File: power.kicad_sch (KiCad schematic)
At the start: 39 parts

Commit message: Annotate schematic
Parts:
- gave numbers to parts that had none: 39
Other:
- moved on the sheet: TP203

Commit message: Clean up BOM
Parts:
- removed C205, C206, C207, C208: 1mF, symbol Device:C
- added C205, C206, C207, C208: 1mF, symbol Device:C_Polarized
- C201: value 100u -> 100uF
- C202: value 470u -> 470uF
- C203, C209, C215, C216, C217, C219: value 100n -> 100nF
- C204, C213: value 1u -> 1uF
- C210: value 1000u -> 1mF
- C211: value 330u -> 330uF
- C212: value 1.5n -> 1nF
- C214: value 10n -> 10nF
- C220: value 4.7u -> 4.7uF
- L201: value 68uH -> 47uH
- renumbered TP202 to TP201, TP201 to TP202
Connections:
- net +12V: now also C209.1, C210.1, C212.2, L201.2, R202.2, TP204.1; no longer F201.1
- net +BATT: now also F201.1, C205.1, C206.1, C207.1, C208.1; no longer C201.1, C203.1, TP202.1, U201.1 (VIN)
- net GND: now also C205.2, C206.2, C207.2, C208.2
- new net: C201.1, C203.1, F201.2, TP202.1, U201.1 (VIN)
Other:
- moved on the sheet: F201, TP202

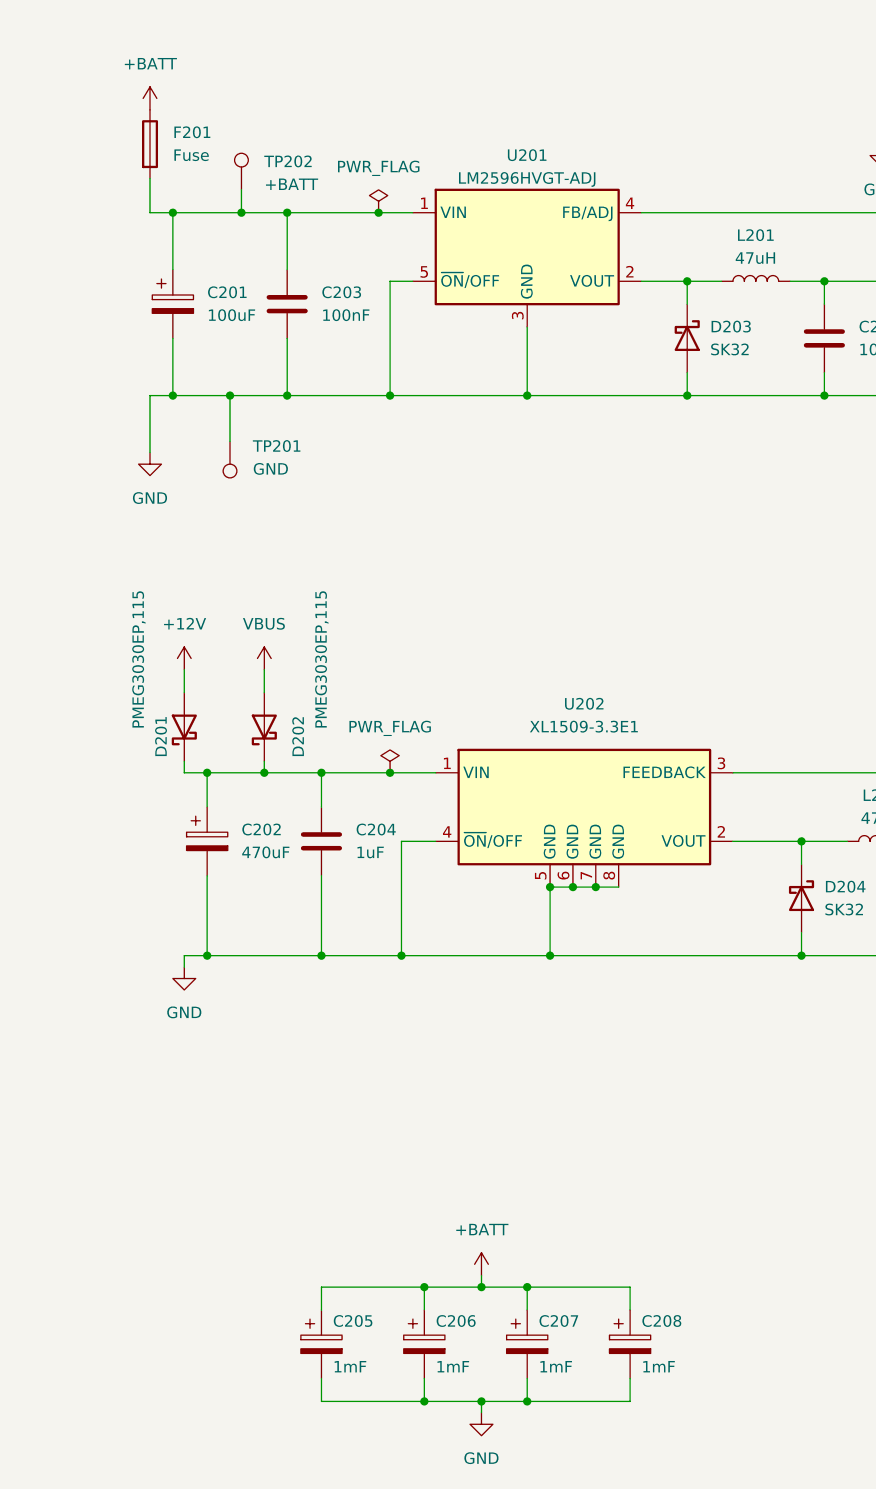
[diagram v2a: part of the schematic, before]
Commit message: Assign footprints
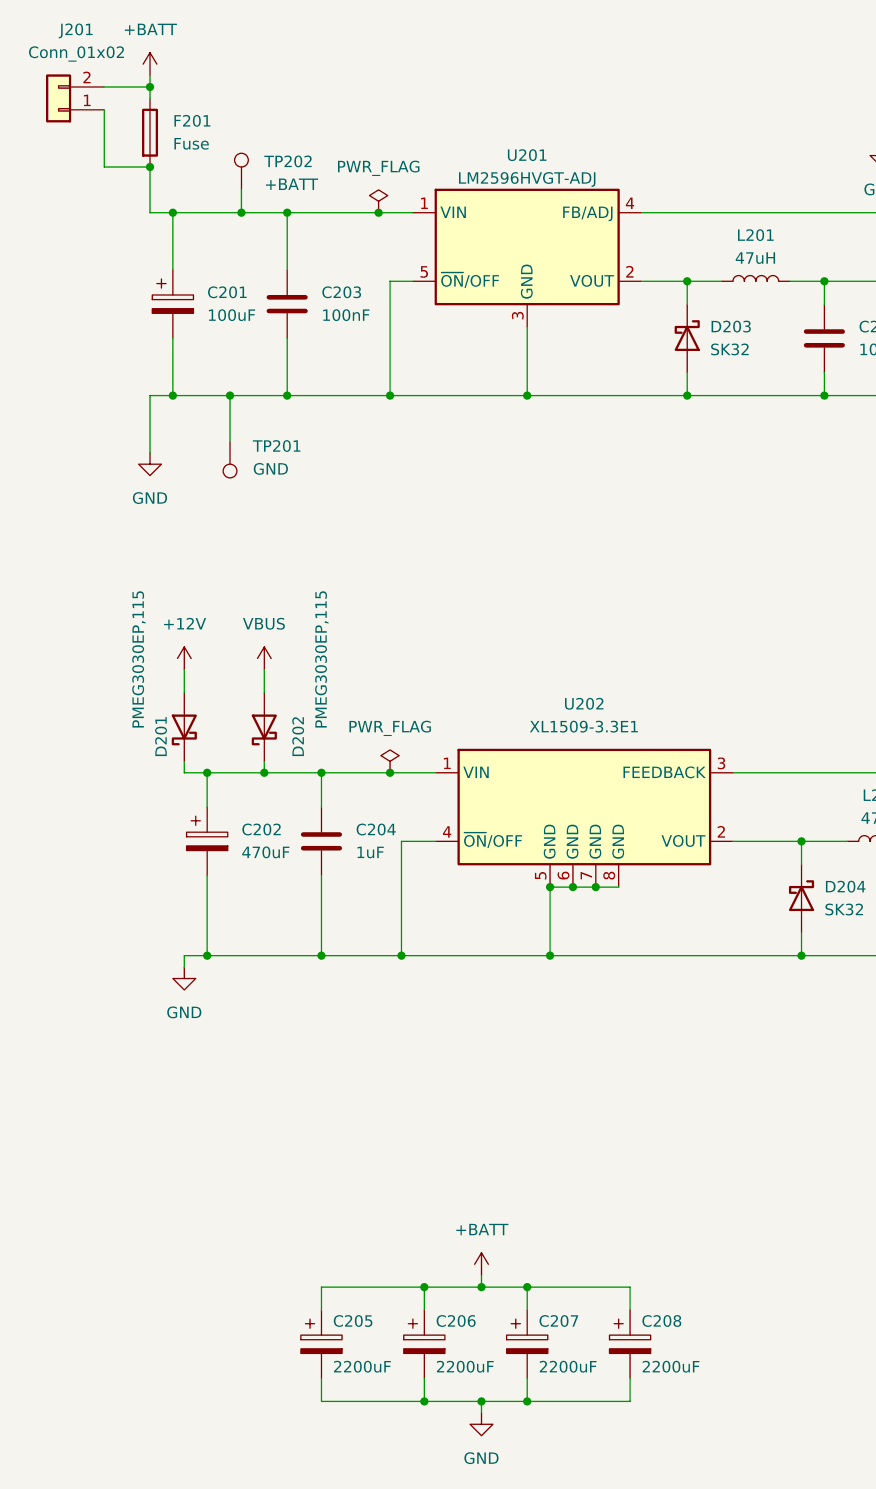
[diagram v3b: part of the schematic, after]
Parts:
- added J201: Conn_01x02, Connector_JST:JST_XH_B2B-XH-A_1x02_P2.50mm_Vertical, symbol Connector_Generic:Conn_01x02
- C201: footprint (none) -> Capacitor_SMD:CP_Elec_10x10.5
- C202: footprint (none) -> Capacitor_SMD:CP_Elec_10x10
- C203, C204, C209, C212, C213, C214, C215, C216, C217, C218, C219, C220: footprint (none) -> Capacitor_SMD:C_0805_2012Metric_Pad1.18x1.45mm_HandSolder
- C205, C206, C207, C208: value 1mF -> 2200uF; footprint (none) -> Capacitor_THT:CP_Radial_D16.0mm_P7.50mm
- C210: footprint (none) -> Capacitor_THT:CP_Radial_D10.0mm_P5.00mm
- C211: footprint (none) -> Capacitor_SMD:CP_Elec_6.3x5.4
- D203, D204: footprint (none) -> Diode_SMD:D_SOD-123F
- F201: footprint (none) -> Fuse:Fuseholder_Littelfuse_Nano2_154x
- L201, L202, L203, R201, R202, R203, R204: footprint (none) -> Resistor_SMD:R_0805_2012Metric_Pad1.20x1.40mm_HandSolder
- TP201, TP202, TP203, TP204: footprint (none) -> TestPoint:TestPoint_Pad_D2.0mm
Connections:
- net +BATT: now also J201.2 (Pin_2)
- net at C201.1, C203.1, F201.2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: now also J201.1 (Pin_1)
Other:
- moved on the sheet: F201

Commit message: Start PCB
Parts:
- removed U203: STM32F103C8Tx, Package_QFP:LQFP-48_7x7mm_P0.5mm, symbol GozLib:STM32F103C8Tx
- added U301: STM32F103C8Tx, Package_QFP:LQFP-48_7x7mm_P0.5mm, symbol GozLib:STM32F103C8Tx
- J201: value Conn_01x02 -> FUSE
- R201, R202, R203, R204: footprint Resistor_SMD:R_0805_2012Metric_Pad1.20x1.40mm_HandSolder -> Resistor_SMD:R_0603_1608Metric_Pad0.98x0.95mm_HandSolder
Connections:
- net +3.3VA: now also U301.9 (VDDA)
- net +3V3: now also U301.1 (VBAT), U301.24 (VDD_1), U301.36 (VDD_2), U301.48 (VDD_3)
- net GND: now also U301.23 (VSS_1), U301.35 (VSS_2), U301.47 (VSS_3), U301.8 (VSSA)
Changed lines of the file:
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@@
       (effects (font (size 1.27 1.27)) (justify left))
     )
-    (property "Footprint" "Resistor_SMD:R_0805_2012Metric_Pad1.20x1.40mm_HandSolder" (id 2) (at 112.522 33.02 90)
+    (property "Footprint" "Resistor_SMD:R_0603_1608Metric_Pad0.98x0.95mm_HandSolder" (id 2) (at 112.522 33.02 90)
       (effects (font (size 1.27 1.27)) hide)
     )
@@
       (effects (font (size 1.27 1.27)) (justify left))
     )
-    (property "Footprint" "Resistor_SMD:R_0805_2012Metric_Pad1.20x1.40mm_HandSolder" (id 2) (at 112.522 40.64 90)
+    (property "Footprint" "Resistor_SMD:R_0603_1608Metric_Pad0.98x0.95mm_HandSolder" (id 2) (at 112.522 40.64 90)
       (effects (font (size 1.27 1.27)) hide)
     )
@@
       (effects (font (size 1.27 1.27)) (justify left))
     )
-    (property "Footprint" "Resistor_SMD:R_0805_2012Metric_Pad1.20x1.40mm_HandSolder" (id 2) (at 252.222 33.02 90)
+    (property "Footprint" "Resistor_SMD:R_0603_1608Metric_Pad0.98x0.95mm_HandSolder" (id 2) (at 252.222 33.02 90)
       (effects (font (size 1.27 1.27)) hide)
     )
@@
       (effects (font (size 1.27 1.27)) (justify left))
     )
-    (property "Footprint" "Resistor_SMD:R_0805_2012Metric_Pad1.20x1.40mm_HandSolder" (id 2) (at 252.222 44.45 90)
+    (property "Footprint" "Resistor_SMD:R_0603_1608Metric_Pad0.98x0.95mm_HandSolder" (id 2) (at 252.222 44.45 90)
       (effects (font (size 1.27 1.27)) hide)
     )
@@
     (in_bom yes) (on_board yes) (fields_autoplaced)
     (property "Reference" "J201" (id 0) (at 18.542 16.51 0))
-    (property "Value" "Conn_01x02" (id 1) (at 18.542 19.05 0))
+    (property "Value" "FUSE" (id 1) (at 18.542 19.05 0))
     (property "Footprint" "Connector_JST:JST_XH_B2B-XH-A_1x02_P2.50mm_Vertical" (id 2) (at 16.51 25.4 0)
       (effects (font (size 1.27 1.27)) hide)
@@
   (symbol (lib_id "GozLib:STM32F103C8Tx") (at 203.2 109.22 0) (unit 2)
     (in_bom yes) (on_board yes) (fields_autoplaced)
-    (property "Reference" "U203" (id 0) (at 203.2 93.98 0))
+    (property "Reference" "U301" (id 0) (at 203.2 93.98 0))
     (property "Value" "STM32F103C8Tx" (id 1) (at 203.2 96.52 0))
-    (property "Footprint" "Package_QFP:LQFP-48_7x7mm_P0.5mm" (id 2) (at 190.5 105.41 0)
-      (effects (font (size 1.27 1.27)) hide)
-    )
-    (property "Datasheet" "http://www.st.com/st-web-ui/static/active/en/resource/technical/document/datasheet/CD00161566.pdf" (id 3) (at 190.5 105.41 0)
-      (effects (font (size 1.27 1.27)) hide)
-    )
+    (property "Footprint" "Package_QFP:LQFP-48_7x7mm_P0.5mm" (id 2) (at 173.99 91.44 0)
+      (effects (font (size 1.27 1.27)) hide)
+    )
+    (property "Datasheet" "http://www.st.com/st-web-ui/static/active/en/resource/technical/document/datasheet/CD00161566.pdf" (id 3) (at 207.01 87.63 0)
+      (effects (font (size 1.27 1.27)) hide)
+    )

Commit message: First PCB commit
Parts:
- added C206, C208, C210, C212: 2200uF, Capacitor_THT:CP_Radial_D18.0mm_P7.50mm, symbol Device:C_Polarized
- C202: footprint Capacitor_SMD:CP_Elec_10x10 -> Capacitor_SMD:CP_Elec_8x10.5
- C203, C204: footprint Capacitor_SMD:C_0805_2012Metric_Pad1.18x1.45mm_HandSolder -> Capacitor_SMD:C_0603_1608Metric_Pad1.08x0.95mm_HandSolder
- C205: footprint Capacitor_THT:CP_Radial_D16.0mm_P7.50mm -> Capacitor_THT:CP_Radial_D18.0mm_P7.50mm
- C207: renamed from C206; footprint Capacitor_THT:CP_Radial_D16.0mm_P7.50mm -> Capacitor_THT:CP_Radial_D18.0mm_P7.50mm
- C209: renamed from C207; footprint Capacitor_THT:CP_Radial_D16.0mm_P7.50mm -> Capacitor_THT:CP_Radial_D18.0mm_P7.50mm
- C211: renamed from C208; footprint Capacitor_THT:CP_Radial_D16.0mm_P7.50mm -> Capacitor_THT:CP_Radial_D18.0mm_P7.50mm
- C213: renamed from C209; footprint Capacitor_SMD:C_0805_2012Metric_Pad1.18x1.45mm_HandSolder -> Capacitor_SMD:C_0603_1608Metric_Pad1.08x0.95mm_HandSolder
- C214: renamed from C210; value 1mF -> 1000uF; footprint Capacitor_THT:CP_Radial_D10.0mm_P5.00mm -> Capacitor_SMD:CP_Elec_10x10.5
- C216: renamed from C212; footprint Capacitor_SMD:C_0805_2012Metric_Pad1.18x1.45mm_HandSolder -> Capacitor_SMD:C_0603_1608Metric_Pad1.08x0.95mm_HandSolder
- C217: renamed from C213; footprint Capacitor_SMD:C_0805_2012Metric_Pad1.18x1.45mm_HandSolder -> Capacitor_SMD:C_0603_1608Metric_Pad1.08x0.95mm_HandSolder
- C218: renamed from C214; footprint Capacitor_SMD:C_0805_2012Metric_Pad1.18x1.45mm_HandSolder -> Capacitor_SMD:C_0603_1608Metric_Pad1.08x0.95mm_HandSolder
- C219: renamed from C215; footprint Capacitor_SMD:C_0805_2012Metric_Pad1.18x1.45mm_HandSolder -> Capacitor_SMD:C_0603_1608Metric_Pad1.08x0.95mm_HandSolder
- C220: renamed from C216; footprint Capacitor_SMD:C_0805_2012Metric_Pad1.18x1.45mm_HandSolder -> Capacitor_SMD:C_0603_1608Metric_Pad1.08x0.95mm_HandSolder
- C221: renamed from C217; footprint Capacitor_SMD:C_0805_2012Metric_Pad1.18x1.45mm_HandSolder -> Capacitor_SMD:C_0603_1608Metric_Pad1.08x0.95mm_HandSolder
- C222: renamed from C218; footprint Capacitor_SMD:C_0805_2012Metric_Pad1.18x1.45mm_HandSolder -> Capacitor_SMD:C_0603_1608Metric_Pad1.08x0.95mm_HandSolder
- C223: renamed from C219; footprint Capacitor_SMD:C_0805_2012Metric_Pad1.18x1.45mm_HandSolder -> Capacitor_SMD:C_0603_1608Metric_Pad1.08x0.95mm_HandSolder
- C224: renamed from C220; footprint Capacitor_SMD:C_0805_2012Metric_Pad1.18x1.45mm_HandSolder -> Capacitor_SMD:C_0603_1608Metric_Pad1.08x0.95mm_HandSolder
- L201, L202: footprint Resistor_SMD:R_0805_2012Metric_Pad1.20x1.40mm_HandSolder -> GozLib:L_10.4x10.4_H4.8_Handsoldering
- L203: footprint Resistor_SMD:R_0805_2012Metric_Pad1.20x1.40mm_HandSolder -> Inductor_SMD:L_0805_2012Metric_Pad1.15x1.40mm_HandSolder
- renumbered C211 to C215, U301 to U203
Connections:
- net +BATT: now also C206.1, C208.1, C210.1, C212.1
- net GND: now also C206.2, C208.2, C210.2, C212.2
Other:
- moved on the sheet: C205, C207, C209, C211

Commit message: Finish regulator layout
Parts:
- C201: footprint Capacitor_SMD:CP_Elec_10x10.5 -> Capacitor_THT:CP_Radial_D8.0mm_P3.50mm
- C214: footprint Capacitor_SMD:CP_Elec_10x10.5 -> Capacitor_THT:CP_Radial_D10.0mm_P5.00mm
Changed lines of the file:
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@@
       (effects (font (size 1.27 1.27)) (justify left))
     )
-    (property "Footprint" "Capacitor_SMD:CP_Elec_10x10.5" (id 2) (at 30.1752 50.8 0)
+    (property "Footprint" "Capacitor_THT:CP_Radial_D8.0mm_P3.50mm" (id 2) (at 30.1752 50.8 0)
       (effects (font (size 1.27 1.27)) hide)
     )
@@
       (effects (font (size 1.27 1.27)) (justify left))
     )
-    (property "Footprint" "Capacitor_SMD:CP_Elec_10x10.5" (id 2) (at 115.2652 54.61 0)
-      (effects (font (size 1.27 1.27)) hide)
-    )
+    (property "Footprint" "Capacitor_THT:CP_Radial_D10.0mm_P5.00mm" (id 2) (at 115.2652 54.61 0)
+      (effects (font (size 1.27 1.27)) hide)
+    )

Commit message: Tweak PCB and add gerbers
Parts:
- added R205, R206: 0R, Resistor_SMD:R_0603_1608Metric_Pad0.98x0.95mm_HandSolder, symbol Device:R
- C205, C206, C207, C208, C209, C210, C211, C212: footprint Capacitor_THT:CP_Radial_D18.0mm_P7.50mm -> GozLib:CP_Radial_D18.0mm_P7.50mm_P5.00mm
- L202: footprint GozLib:L_10.4x10.4_H4.8_Handsoldering -> GozLib:L_YNR6045
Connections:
- net +12V: now also R206.1; no longer C213.1, C214.1, C216.2, L201.2, R202.2, TP204.1
- net +3V3: now also R205.1; no longer C215.1, L202.2, TP203.1, U202.3 (FEEDBACK)
- new net: C213.1, C214.1, C216.2, L201.2, R202.2, R206.2, TP204.1
- new net: C215.1, L202.2, R205.2, TP203.1, U202.3 (FEEDBACK)
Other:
- moved on the sheet: L203
